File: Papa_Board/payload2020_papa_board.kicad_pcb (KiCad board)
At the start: 4 copper layers, 82 x 82 mm, 105 parts, among them J1 1862, J10 1862, J11 Conn_01x05, J2 Conn_01x05, J3 Conn_01x05_Female, J4 Conn_01x05, J5 M80-5000642, J6 M80-5000642, J7 1862, J8 693072010801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

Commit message: Address Lana + Jack's comments on schematic, rename files to "papa board"
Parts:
- R4, R5, R9: value 330R -> 500R
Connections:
- net /+5.3V renamed ~
- C25 pad 1: /+37V -> Net-(C25-Pad1)
- C26 pad 1: /+37V -> Net-(C25-Pad1)
- D1 pad 1: /+37V -> Net-(C25-Pad1)
- J5 pad 2: /+37V -> Net-(J5-Pad2)
- J6 pad 2: /+37V -> Net-(J6-Pad2)
- R11 pad 2: Net-(F5-Pad2) -> +3V3
- R14 pad 1: /+37V -> Net-(C25-Pad1)
- R7 pad 2: Net-(F4-Pad2) -> +BATT
- U1 pad 3: Net-(F4-Pad2) -> +BATT
- U2 pad 3: Net-(F5-Pad2) -> +3V3
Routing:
- added copper zone on B.Cu, net /+5.3V
- added copper zone on F.Cu, net Net-(C25-Pad1)
- added copper zone on VCC.Cu, net Net-(J5-Pad2)
- removed copper zone on F.Cu, net /+37V
- removed copper zone on VCC.Cu, net /+37V

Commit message: Address layout/routing reviews, update gerbers + pdf
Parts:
- removed F4, F5: 400mA, Fuse:Fuse_0805_2012Metric_Pad1.15x1.40mm_HandSolder
- C17: footprint Capacitor_SMD:C_0805_2012Metric_Pad1.18x1.45mm_HandSolder -> Capacitor_SMD:C_0805_2012Metric_Pad1.15x1.40mm_HandSolder
- C25: footprint Capacitor_SMD:C_1206_3216Metric_Pad1.33x1.80mm_HandSolder -> Capacitor_SMD:C_1206_3216Metric_Pad1.42x1.75mm_HandSolder
- R25: footprint Resistor_SMD:R_0805_2012Metric_Pad1.20x1.40mm_HandSolder -> Resistor_SMD:R_0805_2012Metric_Pad1.15x1.40mm_HandSolder
- moved J2 2.09 mm to (141.7, 104.1)
- moved J3 1.80 mm to (147.3, 110.5)
- moved R10 0.43 mm to (177.5, 118.7)
- moved R25 0.15 mm to (178.3, 126.8)
- moved C25 0.10 mm to (124.0, 117.1)
- renumbered DW1 to D3, DR1 to D4, DB1 to D5
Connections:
- net ~ renamed +5.3V
- R11 pad 2: +3V3 -> /battery_management/3V3_OUT
- U2 pad 3: +3V3 -> /battery_management/3V3_OUT
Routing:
- net Net-(F4-Pad2): track 7.06 -> 0.00 mm
- net Net-(F5-Pad2): track 6.41 -> 0.00 mm
- net /battery_management/3V3_OUT: track 0.00 -> 3.86 mm
- net +BATT: track 113.7 -> 116.8 mm
- net +3V3: track 168.8 -> 165.8 mm
- net /CANL_ROCKET: track 83.2 -> 81.1 mm
- net /CANH_ROCKET: track 85.1 -> 83.1 mm
- net GND: track 147.4 -> 145.5 mm, vias 107 -> 103
- net 3V3_CURR_AMP: track 58.7 -> 60.6 mm
- net Net-(J8-Pad7): track 32.1 -> 33.9 mm
- net +5.3V: track 100.4 -> 99.1 mm
- net /ICSPDAT: track 27.8 -> 26.7 mm
- net MAMA_PWR_EN: track 84.3 -> 84.9 mm
- net /+37V: track 0.37 -> 0.00 mm, vias 3 -> 0
- net Net-(C25-Pad1): vias 0 -> 3
- added copper zone on B.Cu, net +5V
- removed copper zone on B.Cu, net /+5.3V
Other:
- board text added: "B"
- board text added: "R"
- board text added: "W"

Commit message: Fix silkscreen
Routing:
- net /5V3_ALWAYS_ON: track 57.4 -> 62.8 mm
- net GND: track 145.5 -> 144.6 mm

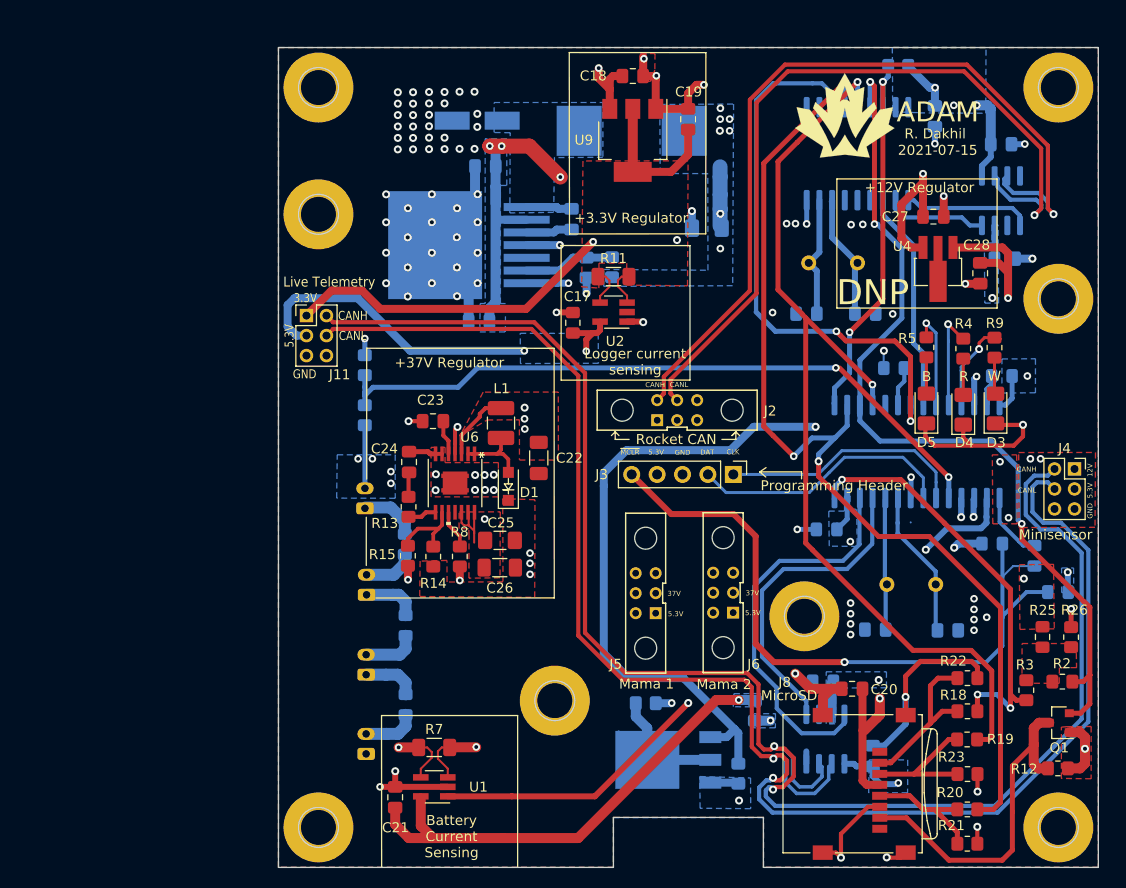
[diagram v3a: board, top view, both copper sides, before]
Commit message: Change battery connector to 10pin JST, fix orientation of SD card, update gerbers + pdf
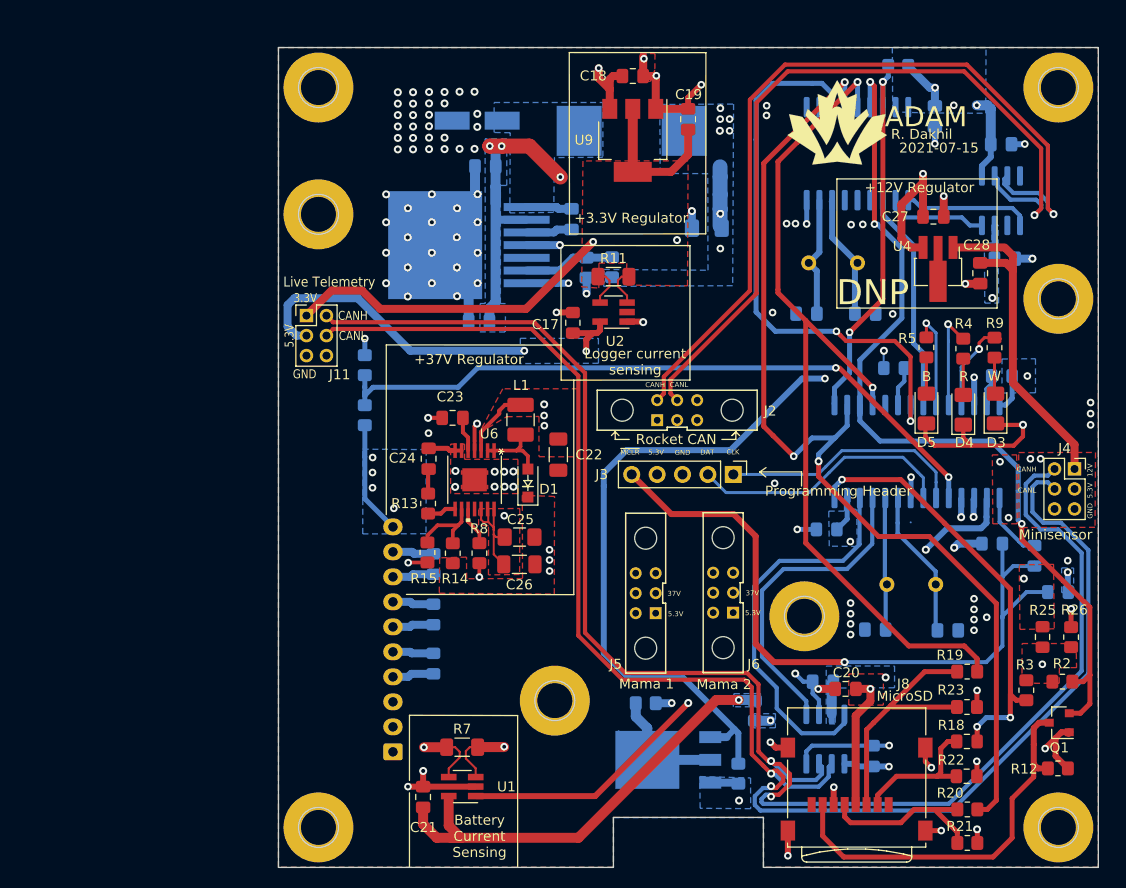
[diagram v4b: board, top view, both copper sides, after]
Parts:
- removed J10, J7, J9: 1862, Connector_JST:JST_PH_S2B-PH-K_1x02_P2.00mm_Horizontal
- J1: value 1862 -> S10B-XH-A(LF)(SN); footprint Connector_JST:JST_PH_S2B-PH-K_1x02_P2.00mm_Horizontal -> Connector_JST:JST_XH_S10B-XH-A_1x10_P2.50mm_Horizontal
- R18, R22: footprint Resistor_SMD:R_0805_2012Metric_Pad1.20x1.40mm_HandSolder -> Resistor_SMD:R_0805_2012Metric_Pad1.15x1.40mm_HandSolder
- moved J1 24.5 mm to (113.3, 138.3)
- moved J8 12.0 mm to (152.8, 146.1), turned to 0 degrees
- moved R22 9.81 mm to (170.7, 140.7)
- moved R19 6.79 mm to (170.7, 130.2)
- moved R23 6.71 mm to (170.7, 133.8)
- moved F3 4.95 mm to (117.3, 129.4), turned to 90 degrees
- moved F1 3.49 mm to (117.4, 119.5), turned to 90 degrees
- moved R18 3.02 mm to (170.7, 137.2)
- moved F2 2.99 mm to (117.3, 124.5), turned to 90 degrees
- moved R7 2.79 mm to (120.2, 137.8)
- moved C21 2.79 mm to (116.3, 142.8)
- moved U1 2.79 mm to (120.2, 141.7)
- moved C23 1.98 mm to (119.3, 104.9)
- moved C25 1.98 mm to (126.0, 116.8)
- moved U6 1.98 mm to (121.5, 111.0)
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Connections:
- net /CANH_PAYLOAD renamed /+
- net /CANL_PAYLOAD renamed /-
- J1 pad 1: Net-(F1-Pad1) -> Net-(J1-Pad1)
- J1 pad 2: +BATT -> Net-(J1-Pad2)
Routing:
- net Net-(J8-Pad3): track 13.5 -> 26.0 mm
- net GND: track 144.6 -> 133.6 mm, vias 103 -> 115
- net /Logger board/MOSI: track 97.2 -> 87.6 mm
- net +3V3: track 165.8 -> 158.9 mm
- net /+: track 165.9 -> 159.8 mm
- net /-: track 166.9 -> 160.9 mm
- net +BATT: track 116.8 -> 122.1 mm
- net Net-(J8-Pad7): track 33.9 -> 39.0 mm
- net Net-(J8-Pad5): track 12.7 -> 17.6 mm
- net +5.3V: track 99.1 -> 96.2 mm
- net BATT_CURR_AMP: track 71.3 -> 68.6 mm
- net /PWR_EN: track 85.6 -> 83.0 mm
- net Net-(J8-Pad2): track 16.7 -> 14.4 mm
- net /5V3_ALWAYS_ON: track 62.8 -> 60.7 mm
- net +12V: track 33.3 -> 35.1 mm, vias 1 -> 0
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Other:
- board text added: "BATT1"
- board text added: "BATT2"
- board text added: "BATT3"
- board text added: "BATT4"
- board text added: "NC"
- board text removed: "BATT_1"
- board text removed: "BATT_2"
- board text removed: "BATT_3"
- board text removed: "BATT_4"

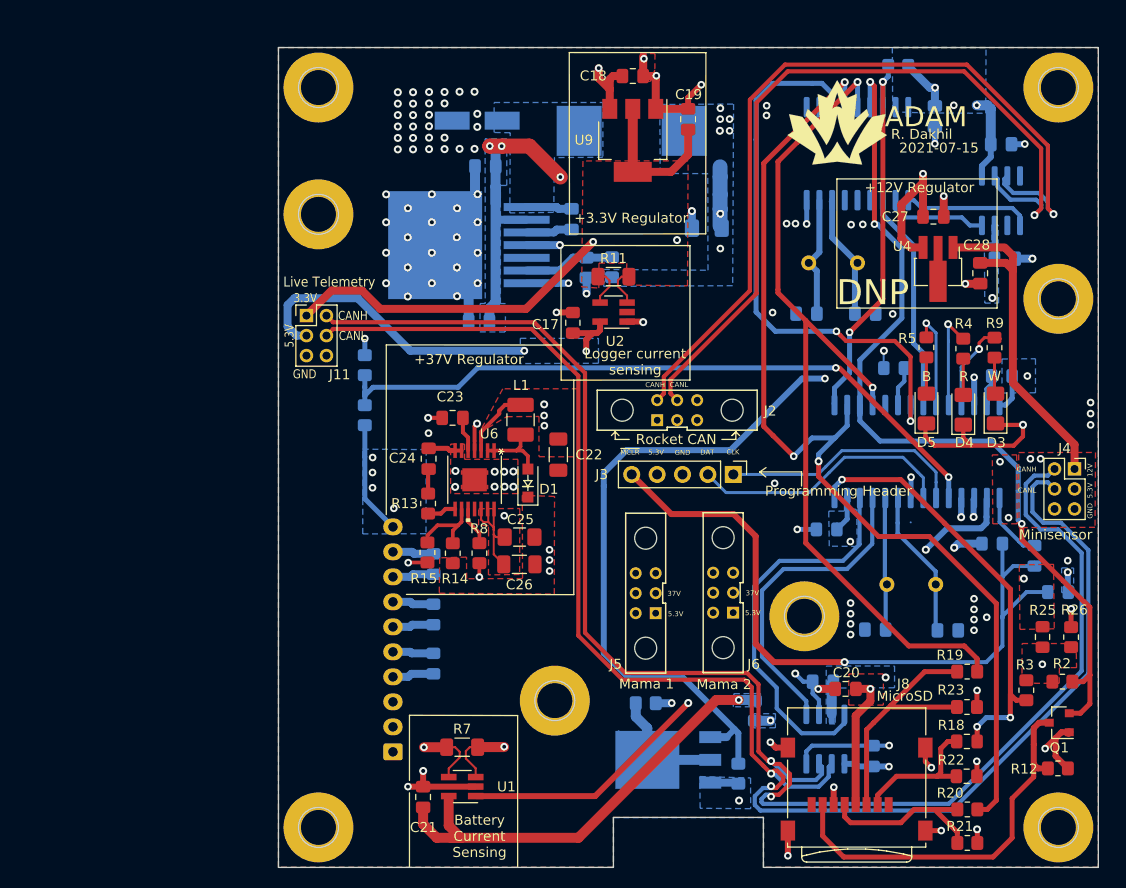
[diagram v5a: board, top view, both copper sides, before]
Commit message: Papa board revision changes (see desc)
- simplify power nets
- change 5.3V buck to 5V
- change 5V buck to b always enabled
- change input voltage to dspic33
- remove live telemetry connector
- add load resistor to 37V boost to keep operation in PWM mode
- fix current sensing lines
- change battery connectors to 2-pin
- PCB layout still needs some work
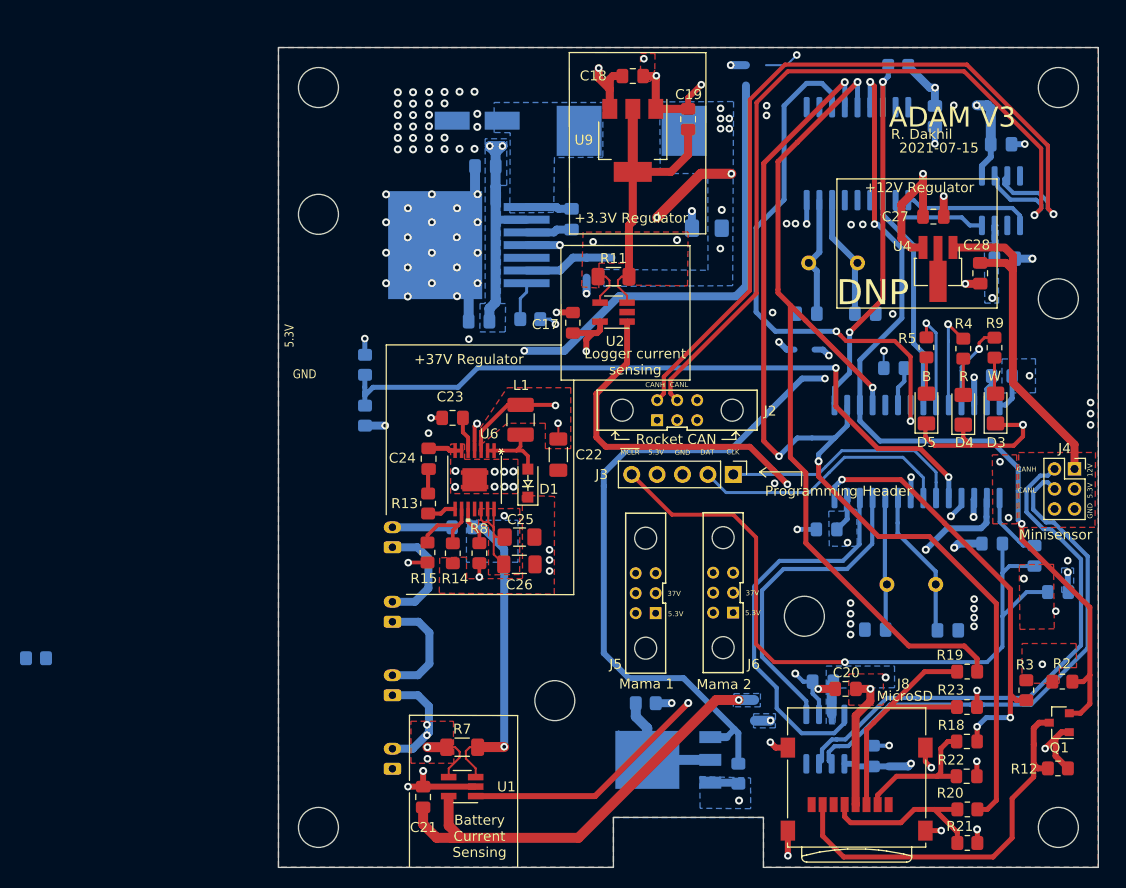
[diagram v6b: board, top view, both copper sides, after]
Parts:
- removed F2, F3: 400mA, Fuse:Fuse_0805_2012Metric_Pad1.15x1.40mm_HandSolder
- removed G***: LOGO, Payload2020_custom:Logo_SilkScreen_10mm
- removed J11: Conn_01x05, Payload2020_custom:PinHeader_2x03_P2.00mm_Vertical_Harwin_Spacing
- removed R17: 330R, Resistor_SMD:R_0805_2012Metric_Pad1.20x1.40mm_HandSolder
- removed R25: 30kR, Resistor_SMD:R_0805_2012Metric_Pad1.15x1.40mm_HandSolder
- removed R26: 5kR, Resistor_SMD:R_0805_2012Metric_Pad1.20x1.40mm_HandSolder
- removed R27: 0R, Resistor_SMD:R_0805_2012Metric_Pad1.20x1.40mm_HandSolder
- removed REF** (x8): MountingHole_3.5mm_Pad, MountingHole:MountingHole_3.5mm_Pad
- added J10: Conn_01x02_Female, Connector_JST:JST_PH_S2B-PH-K_1x02_P2.00mm_Horizontal, B.Cu at (113.3, 139.9)
- added J7: Conn_01x02_Female, Connector_JST:JST_PH_S2B-PH-K_1x02_P2.00mm_Horizontal, B.Cu at (113.3, 125.2)
- added J9: Conn_01x02_Female, Connector_JST:JST_PH_S2B-PH-K_1x02_P2.00mm_Horizontal, B.Cu at (113.3, 132.6)
- added R32: 470kR, Resistor_SMD:R_0805_2012Metric_Pad1.20x1.40mm_HandSolder, B.Cu at (127.0, 95.0)
- C7: value 100uF -> 57uF
- F1: value 400mA -> 500mA
- J1: value S10B-XH-A(LF)(SN) -> Conn_01x02_Female; footprint Connector_JST:JST_XH_S10B-XH-A_1x10_P2.50mm_Horizontal -> Connector_JST:JST_PH_S2B-PH-K_1x02_P2.00mm_Horizontal
- R16: value 20R -> 10kR 0.25W
- U9: value AP2114H-3.3TRG1 -> ZLDO1117QG33TA
- moved R16 69.6 mm to (77.6, 128.9), turned to 180 degrees
- moved J1 20.5 mm to (113.3, 117.8)
- moved F1 4.67 mm to (120.3, 115.8), turned to 0 degrees
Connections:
- net /5.3V_OUT renamed /5V_MAMA
- net /Logger board/MISO renamed /MCU and CAN controllers/MISO
- net /Logger board/MOSI renamed /MCU and CAN controllers/MOSI
- net /Logger board/SCK renamed /MCU and CAN controllers/SCK
- net /~MCLR renamed /~{MCLR}
- C11 pad 2: /5V3_ALWAYS_ON -> +3V3
- C12 pad 1: /5V3_ALWAYS_ON -> +5V
- C13 pad 1: /5V3_ALWAYS_ON -> +5V
- C14 pad 1: /5V3_ALWAYS_ON -> +5V
- C15 pad 1: /5V3_ALWAYS_ON -> +5V
- C16 pad 1: /5V3_ALWAYS_ON -> +5V
- C17 pad 2: +5.3V -> +5V
- C18 pad 2: +5.3V -> +5V
- C19 pad 2: +3V3 -> Net-(C19-Pad2)
- C29 pad 1: /5V3_ALWAYS_ON -> +3V3
- C7 pad 2: +5.3V -> +5V
- J1 pad 2: Net-(J1-Pad2) -> Net-(F1-Pad1)
- J2 pad 1: Net-(J2-Pad1) -> unconnected-(J2-Pad1)
- J2 pad 2: Net-(J2-Pad2) -> unconnected-(J2-Pad2)
- J3 pad 4: +5.3V -> +5V
- J4 pad 2: +5.3V -> +5V
- J5 pad 4: Net-(J5-Pad4) -> unconnected-(J5-Pad4)
- J5 pad 5: Net-(J5-Pad5) -> unconnected-(J5-Pad5)
- J5 pad 6: Net-(J5-Pad6) -> unconnected-(J5-Pad6)
- J6 pad 4: Net-(J6-Pad4) -> unconnected-(J6-Pad4)
- J6 pad 5: Net-(J6-Pad5) -> unconnected-(J6-Pad5)
- J6 pad 6: Net-(J6-Pad6) -> unconnected-(J6-Pad6)
- J8 pad 1: Net-(J8-Pad1) -> unconnected-(J8-Pad1)
- J8 pad 8: Net-(J8-Pad8) -> unconnected-(J8-Pad8)
- L2 pad 2: +5.3V -> +5V
- Q3 pad 3: /5V3_ALWAYS_ON -> +5V
- R1 pad 1: /5V3_ALWAYS_ON -> +5V
- R11 pad 2: /battery_management/3V3_OUT -> Net-(C19-Pad2)
- R16 pad 1: +5.3V -> Net-(C25-Pad1)
- R16 pad 2: Net-(R16-Pad2) -> GND
- R18 pad 2: /Logger board/CS -> /MCU and CAN controllers/CS_2
- R24 pad 1: /5V3_ALWAYS_ON -> +5V
- R6 pad 1: /5V3_ALWAYS_ON -> +3V3
- R7 pad 2: +BATT -> Net-(F1-Pad2)
- U1 pad 3: +BATT -> Net-(F1-Pad2)
- U10 pad 3: /5V3_ALWAYS_ON -> +5V
- U10 pad 5: /5V3_ALWAYS_ON -> +5V
- U2 pad 3: /battery_management/3V3_OUT -> Net-(C19-Pad2)
- U2 pad 5: +5.3V -> +5V
- U3 pad 5: Net-(U3-Pad5) -> unconnected-(U3-Pad5)
- U3 pad 6: Net-(R16-Pad2) -> unconnected-(U3-Pad6)
- U3 pad 7: /PWR_EN -> Net-(R32-Pad2)
- U5 pad 10: Net-(U5-Pad10) -> unconnected-(U5-Pad10)
- U5 pad 11: Net-(U5-Pad11) -> unconnected-(U5-Pad11)
- U5 pad 17: /5V3_ALWAYS_ON -> +5V
- U5 pad 18: /5V3_ALWAYS_ON -> +5V
- U5 pad 4: Net-(U5-Pad4) -> unconnected-(U5-Pad4)
- U5 pad 5: Net-(U5-Pad5) -> unconnected-(U5-Pad5)
- U5 pad 6: Net-(U5-Pad6) -> unconnected-(U5-Pad6)
- U6 pad 11: Net-(U6-Pad11) -> unconnected-(U6-Pad11)
- U6 pad 4: /PWR_EN -> /37V_EN
- U7 pad 3: /5V3_ALWAYS_ON -> +5V
- U7 pad 5: /5V3_ALWAYS_ON -> +5V
- U8 pad 13: /5V3_ALWAYS_ON -> +3V3
- U8 pad 14: /Logger board/CS -> /MCU and CAN controllers/CS_2
- U8 pad 28: /5V3_ALWAYS_ON -> +3V3
- U8 pad 4: /PWR_EN -> /37V_EN
- U9 pad 2: +3V3 -> Net-(C19-Pad2)
- U9 pad 3: +5.3V -> +5V
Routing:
- net +5V: track 0.00 -> 136.0 mm, vias 1 -> 19
- net /-: track 160.9 -> 52.7 mm, vias 2 -> 0
- net /+: track 159.8 -> 53.8 mm, vias 2 -> 0
- net +3V3: track 158.9 -> 67.8 mm, vias 6 -> 11
- net /PWR_EN: track 83.0 -> 0.00 mm, vias 3 -> 0
- net /5V3_ALWAYS_ON: track 60.7 -> 0.00 mm, vias 12 -> 0
- net /37V_EN: track 0.00 -> 56.9 mm, vias 0 -> 2
- net +5.3V: track 96.2 -> 47.1 mm, vias 14 -> 3
- net /Logger board/CS: track 43.5 -> 0.00 mm, vias 3 -> 0
- net /MCU and CAN controllers/CS_2: track 0.00 -> 43.5 mm, vias 0 -> 3
- net Net-(C19-Pad2): track 0.00 -> 29.5 mm
- net Net-(F1-Pad2): track 4.14 -> 30.9 mm, vias 0 -> 1
- net GND: track 133.6 -> 118.5 mm, vias 115 -> 114
- net Net-(J7-Pad1): track 0.00 -> 11.4 mm
- net Net-(J1-Pad1): track 0.00 -> 11.2 mm
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- added copper zone on B.Cu, net +3V3
- added copper zone on In2.Cu, net +3V3
- added copper zone on In2.Cu, net +5V
- added copper zone on In2.Cu, net +BATT
- added copper zone on In2.Cu, net /5V_MAMA
- added copper zone on In1.Cu, net GND
- added copper zone on B.Cu, net Net-(F1-Pad2)
- added copper zone on In2.Cu, net Net-(J5-Pad2)
- removed copper zone on B.Cu, net +5.3V
- removed copper zone on VCC.Cu, net +5.3V
- removed copper zone on VCC.Cu, net +BATT
- removed copper zone on B.Cu, net /5V3_ALWAYS_ON
- removed copper zone on VCC.Cu, net /5V3_ALWAYS_ON
- removed copper zone on VCC.Cu, net /5V_MAMA
- removed copper zone on GND.Cu, net GND
- removed copper zone on VCC.Cu, net Net-(J5-Pad2)
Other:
- net class Default removed
- board text added: "ADAM V3"
- board text added: "~{MCLR}"
- board text removed: "3.3V"
- board text removed: "ADAM"
- board text removed: "Live Telemetry"
- board text removed: "NC"
- board text removed: "~MCLR"
